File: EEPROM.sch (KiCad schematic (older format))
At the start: 0 parts

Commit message: EEPROM schematics were drawn
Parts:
- added C?: C_Small, Capacitor_SMD:C_0603_1608Metric_Pad1.08x0.95mm_HandSolder, symbol Device:C_Small
- added C?: 100nF, Capacitor_SMD:C_0603_1608Metric_Pad1.08x0.95mm_HandSolder, symbol Device:C_Small
- added C?: 30pF, Capacitor_SMD:C_0603_1608Metric_Pad1.08x0.95mm_HandSolder, symbol Device:C_Small
- added IC?: M24M02-DRMN6TP, SOIC127P600X175-8N, symbol GM_Memory_EEPROM:M24M02-DRMN6TP
- added R?: R_Small_US, Resistor_SMD:R_0603_1608Metric_Pad0.98x0.95mm_HandSolder, symbol Device:R_Small_US
- added R?: 0, Resistor_SMD:R_0603_1608Metric_Pad0.98x0.95mm_HandSolder, symbol Device:R_Small_US
- added R?: 4K, Resistor_SMD:R_0603_1608Metric_Pad0.98x0.95mm_HandSolder, symbol Device:R_Small_US
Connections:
- net labels added: +3V3, EEPROM_SCL, EEPROM_SDA, EEPROM_WC, GNDD, VCC3V3
- wire segments 0 -> 24
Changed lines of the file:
@@
 Comment4 ""
 $EndDescr
+$Comp
+L GM_Memory_EEPROM:M24M02-DRMN6TP IC?
+U 1 1 601D69D3
+P 3850 3300
+F 0 "IC?" H 4300 3465 50  0000 C CNN
+F 1 "M24M02-DRMN6TP" H 4300 3374 50  0000 C CNN
+F 2 "SOIC127P600X175-8N" H 5700 3500 50  0001 L CNN
+F 3 "http://www.st.com/content/ccc/resource/technical/document/datasheet/b7/de/9b/f6/03/28/4e/8e/CD00290537.pdf/files/CD00290537.pdf/jcr:content/translations/en.CD00290537.pdf" H 5700 3400 50  0001 L CNN
+F 4 "M24M02-DRMN6TP" H 3850 3300 50  0001 C CNN "MPN"
+	1    3850 3300
+	1    0    0    -1
+$EndComp
+$Comp
+L power:GNDD #PWR?
+U 1 1 601D83DB
+P 5150 4050
+AR Path="/601DF0A6/601D83DB" Ref="#PWR?"  Part="1"
+AR Path="/601E7C5A/601D83DB" Ref="#PWR?"  Part="1"
+F 0 "#PWR?" H 5150 3800 50  0001 C CNN
+F 1 "GNDD" H 5154 3895 50  0000 C CNN
+F 2 "" H 5150 4050 50  0001 C CNN
+F 3 "" H 5150 4050 50  0001 C CNN
+	1    5150 4050
+	1    0    0    -1
+$EndComp
+Wire Wire Line
+	4950 3700 5150 3700
+Wire Wire Line
+	5150 3700 5150 3800
+Wire Wire Line
+	4950 3900 5150 3900
+Connection ~ 5150 3900
+Wire Wire Line
+	5150 3900 5150 4050
+Wire Wire Line
+	4950 3800 5150 3800
+Connection ~ 5150 3800
+Wire Wire Line
+	5150 3800 5150 3900
+Wire Wire Line
+	4950 3400 6000 3400
+Wire Wire Line
+	3650 3400 3500 3400
+Wire Wire Line
+	3650 3800 2500 3800
+Wire Wire Line
+	3650 3900 2500 3900
+$Comp
+L Device:C_Small C?
+U 1 1 601D8FE6
+P 1250 1500
+F 0 "C?" H 1342 1546 50  0000 L CNN
+F 1 "C_Small" H 1342 1455 50  0000 L CNN
+F 2 "Capacitor_SMD:C_0603_1608Metric_Pad1.08x0.95mm_HandSolder" H 1250 1500 50  0001 C CNN
+F 3 "~" H 1250 1500 50  0001 C CNN
+F 4 "" H 1250 1500 50  0000 C CNN "Voltage"
+	1    1250 1500
+	1    0    0    -1
+$EndComp
+$Comp
+L Device:R_Small_US R?
+U 1 1 601D9F52
+P 1950 1500
+F 0 "R?" H 2018 1546 50  0000 L CNN
+F 1 "R_Small_US" H 2018 1455 50  0000 L CNN
+F 2 "Resistor_SMD:R_0603_1608Metric_Pad0.98x0.95mm_HandSolder" H 1950 1500 50  0001 C CNN
+F 3 "~" H 1950 1500 50  0001 C CNN
+	1    1950 1500
+	1    0    0    -1
+$EndComp
+$Comp
+L Device:C_Small C?
+U 1 1 601DC16C
+P 3100 3050
+F 0 "C?" H 3008 2959 50  0000 R CNN
+F 1 "100nF" H 3008 3050 50  0000 R CNN
+F 2 "Capacitor_SMD:C_0603_1608Metric_Pad1.08x0.95mm_HandSolder" H 3100 3050 50  0001 C CNN
+F 3 "~" H 3100 3050 50  0001 C CNN
+F 4 "25V" H 3008 3141 50  0000 R CNN "Voltage"
+	1    3100 3050
+	-1   0    0    1
+$EndComp
+Wire Wire Line
+	3100 2950 3100 2900
+Wire Wire Line
+	3100 2900 3500 2900
+$Comp
+L power:GNDD #PWR?
+U 1 1 601DF224
+P 3100 3200
+AR Path="/601DF0A6/601DF224" Ref="#PWR?"  Part="1"
+AR Path="/601E7C5A/601DF224" Ref="#PWR?"  Part="1"
+F 0 "#PWR?" H 3100 2950 50  0001 C CNN
+F 1 "GNDD" H 3104 3045 50  0000 C CNN
+F 2 "" H 3100 3200 50  0001 C CNN
+F 3 "" H 3100 3200 50  0001 C CNN
+	1    3100 3200
+	1    0    0    -1
+$EndComp
+Wire Wire Line
+	3100 3200 3100 3150
+Text Label 2750 3800 0    50   ~ 0
+EEPROM_SCL
+Text Label 2750 3900 0    50   ~ 0
+EEPROM_SDA
+Text Label 5250 3400 0    50   ~ 0
+EEPROM_WC
+Wire Wire Line
+	3500 2800 3500 2900
+Wire Wire Line
+	3500 2900 3500 3400
+$Comp
+L Device:R_Small_US R?
+U 1 1 601E53C9
+P 2850 3500
+F 0 "R?" V 3050 3500 50  0000 C CNN
+F 1 "0" V 2950 3500 50  0000 C CNN
+F 2 "Resistor_SMD:R_0603_1608Metric_Pad0.98x0.95mm_HandSolder" H 2850 3500 50  0001 C CNN
+F 3 "~" H 2850 3500 50  0001 C CNN
+F 4 "DNP" V 2750 3500 50  0000 C CNN "DNP"
+	1    2850 3500
+	0    -1   -1   0
+$EndComp
+Wire Wire Line
+	3650 3500 2950 3500
+$Comp
+L power:GNDD #PWR?
+U 1 1 601E70A9
+P 2500 3550
+AR Path="/601DF0A6/601E70A9" Ref="#PWR?"  Part="1"
+AR Path="/601E7C5A/601E70A9" Ref="#PWR?"  Part="1"
+F 0 "#PWR?" H 2500 3300 50  0001 C CNN
+F 1 "GNDD" H 2504 3395 50  0000 C CNN
+F 2 "" H 2500 3550 50  0001 C CNN
+F 3 "" H 2500 3550 50  0001 C CNN
+	1    2500 3550
+	1    0    0    -1
+$EndComp
+Wire Wire Line
+	2500 3500 2500 3550
+Wire Wire Line
+	2500 3500 2750 3500
+$Comp
+L Device:R_Small_US R?
+U 1 1 601EAD0F
+P 7900 3150
+F 0 "R?" H 7968 3196 50  0000 L CNN
+F 1 "4K" H 7968 3105 50  0000 L CNN
+F 2 "Resistor_SMD:R_0603_1608Metric_Pad0.98x0.95mm_HandSolder" H 7900 3150 50  0001 C CNN
+F 3 "~" H 7900 3150 50  0001 C CNN
+	1    7900 3150
+	1    0    0    -1
+$EndComp
+Wire Wire Line
+	7900 3250 7900 3400
+Wire Wire Line
+	7900 3050 7900 2900
+Wire Wire Line
+	7900 3750 7900 3950
+Wire Wire Line
+	7900 3400 9000 3400
+Connection ~ 7900 3400
+Text Label 8250 3400 0    50   ~ 0
+EEPROM_SDA
+Wire Wire Line
+	7900 3400 7900 3550
+$Comp
+L Device:C_Small C?
+U 1 1 601EAD09
+P 7900 3650
+F 0 "C?" H 7992 3741 50  0000 L CNN
+F 1 "30pF" H 7992 3650 50  0000 L CNN
+F 2 "Capacitor_SMD:C_0603_1608Metric_Pad1.08x0.95mm_HandSolder" H 7900 3650 50  0001 C CNN
+F 3 "~" H 7900 3650 50  0001 C CNN
+F 4 "25V" H 7992 3559 50  0000 L CNN "Voltage"
+	1    7900 3650
+	1    0    0    -1
+$EndComp
+$Comp
+L power:GNDD #PWR?
+U 1 1 601F091A
+P 7900 3950
+AR Path="/601DF0A6/601F091A" Ref="#PWR?"  Part="1"
+AR Path="/601E7C5A/601F091A" Ref="#PWR?"  Part="1"
+F 0 "#PWR?" H 7900 3700 50  0001 C CNN
+F 1 "GNDD" H 7904 3795 50  0000 C CNN
+F 2 "" H 7900 3950 50  0001 C CNN
+F 3 "" H 7900 3950 50  0001 C CNN
+	1    7900 3950
+	1    0    0    -1
+$EndComp
+$Comp
+L power:PWR_FLAG #FLG?
+U 1 1 601F6B98
+P 1250 1000
+AR Path="/601DF0A6/601F6B98" Ref="#FLG?"  Part="1"
+AR Path="/601E7C5A/601F6B98" Ref="#FLG?"  Part="1"
+F 0 "#FLG?" H 1250 1075 50  0001 C CNN
+F 1 "PWR_FLAG" H 1250 1173 50  0000 C CNN
+F 2 "" H 1250 1000 50  0001 C CNN
+F 3 "~" H 1250 1000 50  0001 C CNN
+	1    1250 1000
+	1    0    0    -1
+$EndComp
+Text GLabel 1050 1000 0    50   Input ~ 0
+VCC3V3
+Wire Wire Line
+	1050 1000 1250 1000
+Text HLabel 6000 3400 2    50   Input ~ 0
+EEPROM_WC
+Text HLabel 2500 3900 0    50   Input ~ 0
+EEPROM_SDA
+Text HLabel 2500 3800 0    50   Input ~ 0
+EEPROM_SCL
+$Comp
+L power:+3V3 #PWR?
+U 1 1 601FBA69
+P 3500 2800
+F 0 "#PWR?" H 3500 2650 50  0001 C CNN
+F 1 "+3V3" H 3515 2973 50  0000 C CNN
+F 2 "" H 3500 2800 50  0001 C CNN
+F 3 "" H 3500 2800 50  0001 C CNN
+	1    3500 2800
+	1    0    0    -1
+$EndComp
+$Comp
+L power:+3V3 #PWR?
+U 1 1 601FC8B2
+P 7900 2900
+F 0 "#PWR?" H 7900 2750 50  0001 C CNN
+F 1 "+3V3" H 7915 3073 50  0000 C CNN
+F 2 "" H 7900 2900 50  0001 C CNN
+F 3 "" H 7900 2900 50  0001 C CNN
+	1    7900 2900
+	1    0    0    -1
+$EndComp
+Connection ~ 3500 2900
 $EndSCHEMATC

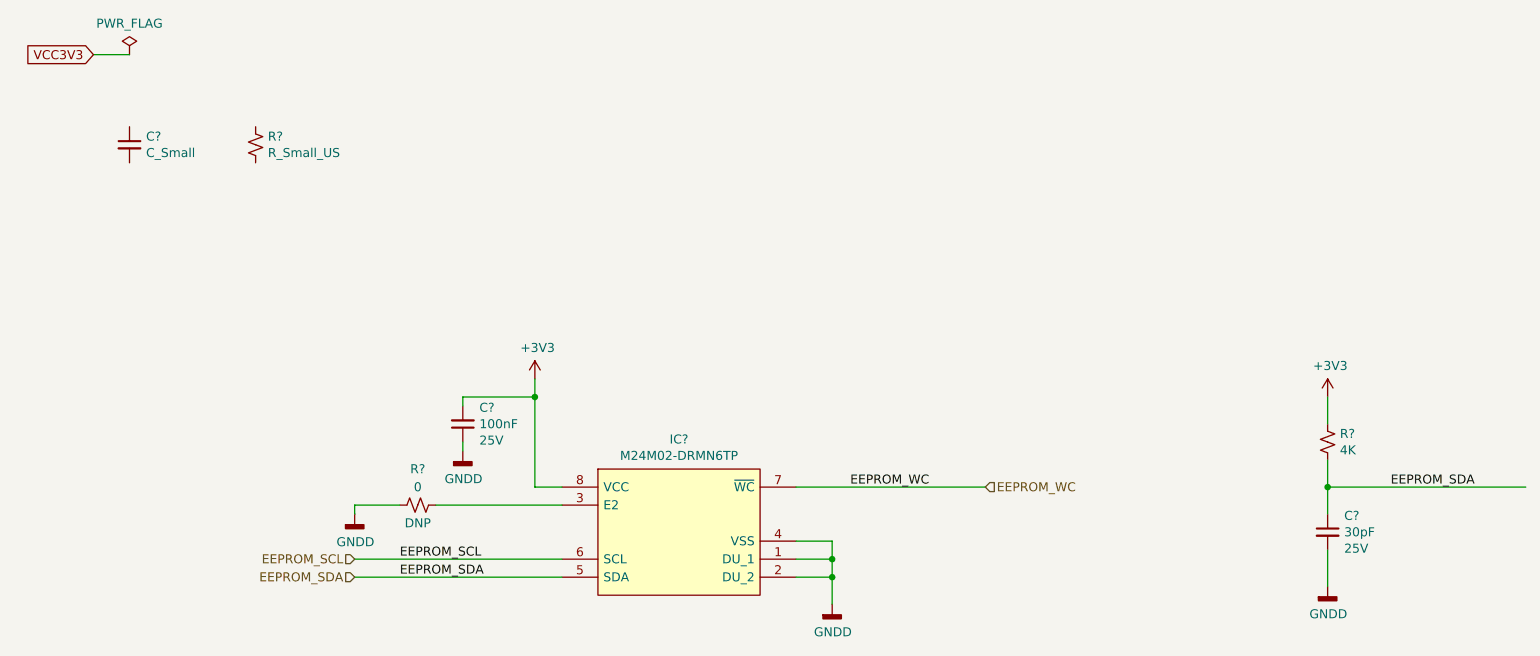
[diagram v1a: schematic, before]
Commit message: Completeed the FPGA_Power sheet Created PCB
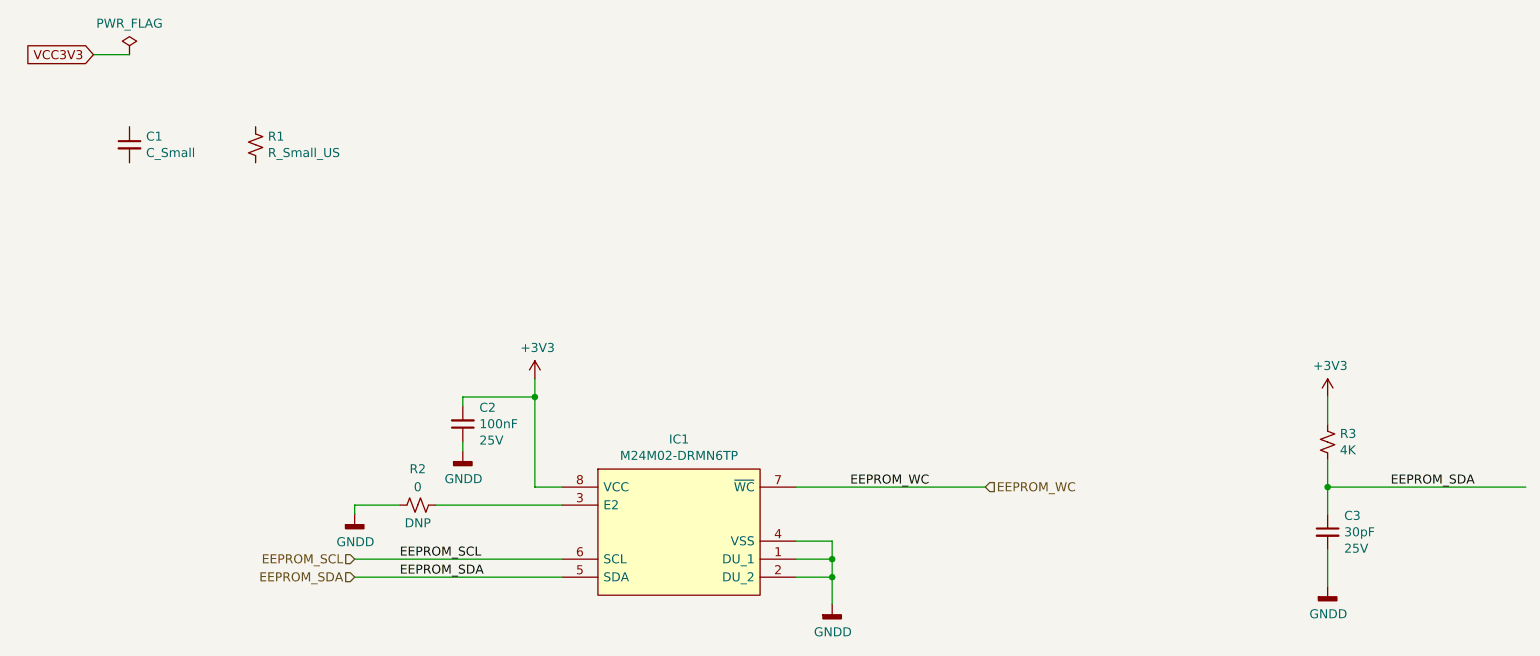
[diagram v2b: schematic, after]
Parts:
- gave numbers to parts that had none: 7
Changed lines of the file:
@@
 $EndDescr
 $Comp
-L GM_Memory_EEPROM:M24M02-DRMN6TP IC?
+L GM_Memory_EEPROM:M24M02-DRMN6TP IC1
 U 1 1 601D69D3
 P 3850 3300
-F 0 "IC?" H 4300 3465 50  0000 C CNN
+F 0 "IC1" H 4300 3465 50  0000 C CNN
 F 1 "M24M02-DRMN6TP" H 4300 3374 50  0000 C CNN
 F 2 "SOIC127P600X175-8N" H 5700 3500 50  0001 L CNN
@@
 P 5150 4050
 AR Path="/601DF0A6/601D83DB" Ref="#PWR?"  Part="1"
-AR Path="/601E7C5A/601D83DB" Ref="#PWR?"  Part="1"
-F 0 "#PWR?" H 5150 3800 50  0001 C CNN
+AR Path="/601E7C5A/601D83DB" Ref="#PWR04"  Part="1"
+F 0 "#PWR04" H 5150 3800 50  0001 C CNN
 F 1 "GNDD" H 5154 3895 50  0000 C CNN
 F 2 "" H 5150 4050 50  0001 C CNN
@@
 	3650 3900 2500 3900
 $Comp
-L Device:C_Small C?
+L Device:C_Small C1
 U 1 1 601D8FE6
 P 1250 1500
-F 0 "C?" H 1342 1546 50  0000 L CNN
+F 0 "C1" H 1342 1546 50  0000 L CNN
 F 1 "C_Small" H 1342 1455 50  0000 L CNN
 F 2 "Capacitor_SMD:C_0603_1608Metric_Pad1.08x0.95mm_HandSolder" H 1250 1500 50  0001 C CNN
@@
 $EndComp
 $Comp
-L Device:R_Small_US R?
+L Device:R_Small_US R1
 U 1 1 601D9F52
 P 1950 1500
-F 0 "R?" H 2018 1546 50  0000 L CNN
+F 0 "R1" H 2018 1546 50  0000 L CNN
 F 1 "R_Small_US" H 2018 1455 50  0000 L CNN
 F 2 "Resistor_SMD:R_0603_1608Metric_Pad0.98x0.95mm_HandSolder" H 1950 1500 50  0001 C CNN
@@
 $EndComp
 $Comp
-L Device:C_Small C?
+L Device:C_Small C2
 U 1 1 601DC16C
 P 3100 3050
-F 0 "C?" H 3008 2959 50  0000 R CNN
+F 0 "C2" H 3008 2959 50  0000 R CNN
 F 1 "100nF" H 3008 3050 50  0000 R CNN
 F 2 "Capacitor_SMD:C_0603_1608Metric_Pad1.08x0.95mm_HandSolder" H 3100 3050 50  0001 C CNN
@@
 P 3100 3200
 AR Path="/601DF0A6/601DF224" Ref="#PWR?"  Part="1"
-AR Path="/601E7C5A/601DF224" Ref="#PWR?"  Part="1"
-F 0 "#PWR?" H 3100 2950 50  0001 C CNN
+AR Path="/601E7C5A/601DF224" Ref="#PWR02"  Part="1"
+F 0 "#PWR02" H 3100 2950 50  0001 C CNN
 F 1 "GNDD" H 3104 3045 50  0000 C CNN
 F 2 "" H 3100 3200 50  0001 C CNN
@@
 	3500 2900 3500 3400
 $Comp
-L Device:R_Small_US R?
+L Device:R_Small_US R2
 U 1 1 601E53C9
 P 2850 3500
-F 0 "R?" V 3050 3500 50  0000 C CNN
+F 0 "R2" V 3050 3500 50  0000 C CNN
 F 1 "0" V 2950 3500 50  0000 C CNN
 F 2 "Resistor_SMD:R_0603_1608Metric_Pad0.98x0.95mm_HandSolder" H 2850 3500 50  0001 C CNN
@@
 P 2500 3550
 AR Path="/601DF0A6/601E70A9" Ref="#PWR?"  Part="1"
-AR Path="/601E7C5A/601E70A9" Ref="#PWR?"  Part="1"
-F 0 "#PWR?" H 2500 3300 50  0001 C CNN
+AR Path="/601E7C5A/601E70A9" Ref="#PWR01"  Part="1"
+F 0 "#PWR01" H 2500 3300 50  0001 C CNN
 F 1 "GNDD" H 2504 3395 50  0000 C CNN
 F 2 "" H 2500 3550 50  0001 C CNN
@@
 	2500 3500 2750 3500
 $Comp
-L Device:R_Small_US R?
+L Device:R_Small_US R3
 U 1 1 601EAD0F
 P 7900 3150
-F 0 "R?" H 7968 3196 50  0000 L CNN
+F 0 "R3" H 7968 3196 50  0000 L CNN
 F 1 "4K" H 7968 3105 50  0000 L CNN
 F 2 "Resistor_SMD:R_0603_1608Metric_Pad0.98x0.95mm_HandSolder" H 7900 3150 50  0001 C CNN
@@
 	7900 3400 7900 3550
 $Comp
-L Device:C_Small C?
+L Device:C_Small C3
 U 1 1 601EAD09
 P 7900 3650
-F 0 "C?" H 7992 3741 50  0000 L CNN
+F 0 "C3" H 7992 3741 50  0000 L CNN
 F 1 "30pF" H 7992 3650 50  0000 L CNN
 F 2 "Capacitor_SMD:C_0603_1608Metric_Pad1.08x0.95mm_HandSolder" H 7900 3650 50  0001 C CNN
@@
 P 7900 3950
 AR Path="/601DF0A6/601F091A" Ref="#PWR?"  Part="1"
-AR Path="/601E7C5A/601F091A" Ref="#PWR?"  Part="1"
-F 0 "#PWR?" H 7900 3700 50  0001 C CNN
+AR Path="/601E7C5A/601F091A" Ref="#PWR06"  Part="1"
+F 0 "#PWR06" H 7900 3700 50  0001 C CNN
 F 1 "GNDD" H 7904 3795 50  0000 C CNN
 F 2 "" H 7900 3950 50  0001 C CNN
@@
 P 1250 1000
 AR Path="/601DF0A6/601F6B98" Ref="#FLG?"  Part="1"
-AR Path="/601E7C5A/601F6B98" Ref="#FLG?"  Part="1"
-F 0 "#FLG?" H 1250 1075 50  0001 C CNN
+AR Path="/601E7C5A/601F6B98" Ref="#FLG01"  Part="1"
+F 0 "#FLG01" H 1250 1075 50  0001 C CNN
 F 1 "PWR_FLAG" H 1250 1173 50  0000 C CNN
 F 2 "" H 1250 1000 50  0001 C CNN
@@
 EEPROM_SCL
 $Comp
-L power:+3V3 #PWR?
+L power:+3V3 #PWR03
 U 1 1 601FBA69
 P 3500 2800
-F 0 "#PWR?" H 3500 2650 50  0001 C CNN
+F 0 "#PWR03" H 3500 2650 50  0001 C CNN
 F 1 "+3V3" H 3515 2973 50  0000 C CNN
 F 2 "" H 3500 2800 50  0001 C CNN
@@
 $EndComp
 $Comp
-L power:+3V3 #PWR?
+L power:+3V3 #PWR05
 U 1 1 601FC8B2
 P 7900 2900
-F 0 "#PWR?" H 7900 2750 50  0001 C CNN
+F 0 "#PWR05" H 7900 2750 50  0001 C CNN
 F 1 "+3V3" H 7915 3073 50  0000 C CNN
 F 2 "" H 7900 2900 50  0001 C CNN

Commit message: Added power symbol to EEPROM sheet
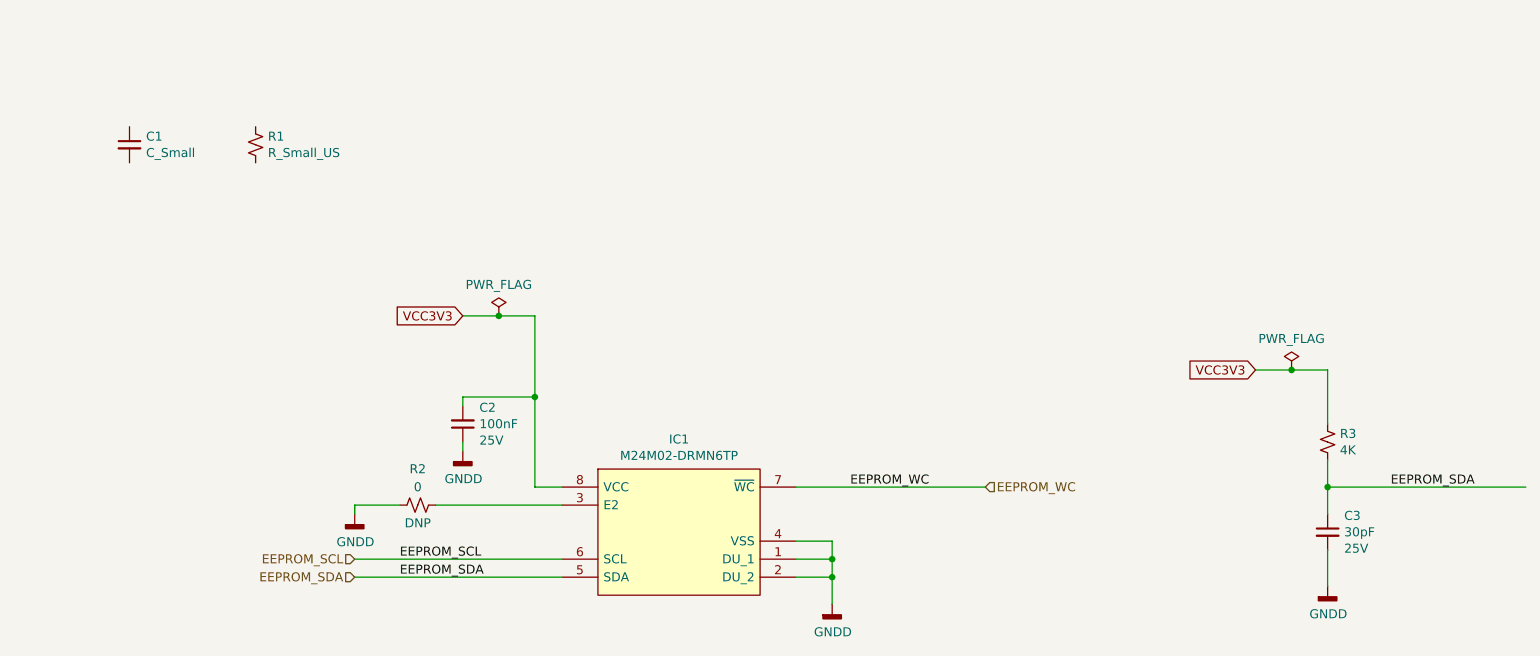
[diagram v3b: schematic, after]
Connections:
- net labels removed: +3V3
- wire segments 24 -> 27
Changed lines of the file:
@@
 EEPROM_WC
-Wire Wire Line
-	3500 2800 3500 2900
 Wire Wire Line
 	3500 2900 3500 3400
@@
 	7900 3250 7900 3400
 Wire Wire Line
-	7900 3050 7900 2900
-Wire Wire Line
 	7900 3750 7900 3950
 Wire Wire Line
@@
 	1    0    0    -1
 $EndComp
-$Comp
-L power:PWR_FLAG #FLG?
-U 1 1 601F6B98
-P 1250 1000
-AR Path="/601DF0A6/601F6B98" Ref="#FLG?"  Part="1"
-AR Path="/601E7C5A/601F6B98" Ref="#FLG01"  Part="1"
-F 0 "#FLG01" H 1250 1075 50  0001 C CNN
-F 1 "PWR_FLAG" H 1250 1173 50  0000 C CNN
-F 2 "" H 1250 1000 50  0001 C CNN
-F 3 "~" H 1250 1000 50  0001 C CNN
-	1    1250 1000
-	1    0    0    -1
-$EndComp
-Text GLabel 1050 1000 0    50   Input ~ 0
-VCC3V3
-Wire Wire Line
-	1050 1000 1250 1000
 Text HLabel 6000 3400 2    50   Input ~ 0
 EEPROM_WC
@@
 Text HLabel 2500 3800 0    50   Input ~ 0
 EEPROM_SCL
+Connection ~ 3500 2900
+Text GLabel 3100 2450 0    50   Input ~ 0
+VCC3V3
 $Comp
-L power:+3V3 #PWR03
-U 1 1 601FBA69
-P 3500 2800
-F 0 "#PWR03" H 3500 2650 50  0001 C CNN
-F 1 "+3V3" H 3515 2973 50  0000 C CNN
-F 2 "" H 3500 2800 50  0001 C CNN
-F 3 "" H 3500 2800 50  0001 C CNN
-	1    3500 2800
+L power:PWR_FLAG #FLG?
+U 1 1 60222E62
+P 3300 2450
+F 0 "#FLG?" H 3300 2525 50  0001 C CNN
+F 1 "PWR_FLAG" H 3300 2623 50  0000 C CNN
+F 2 "" H 3300 2450 50  0001 C CNN
+F 3 "~" H 3300 2450 50  0001 C CNN
+	1    3300 2450
 	1    0    0    -1
 $EndComp
+Wire Wire Line
+	3500 2450 3500 2900
+Connection ~ 3300 2450
+Wire Wire Line
+	3300 2450 3500 2450
+Wire Wire Line
+	3100 2450 3300 2450
+Text GLabel 7500 2750 0    50   Input ~ 0
+VCC3V3
 $Comp
-L power:+3V3 #PWR05
-U 1 1 601FC8B2
-P 7900 2900
-F 0 "#PWR05" H 7900 2750 50  0001 C CNN
-F 1 "+3V3" H 7915 3073 50  0000 C CNN
-F 2 "" H 7900 2900 50  0001 C CNN
-F 3 "" H 7900 2900 50  0001 C CNN
-	1    7900 2900
+L power:PWR_FLAG #FLG?
+U 1 1 602261D1
+P 7700 2750
+F 0 "#FLG?" H 7700 2825 50  0001 C CNN
+F 1 "PWR_FLAG" H 7700 2923 50  0000 C CNN
+F 2 "" H 7700 2750 50  0001 C CNN
+F 3 "~" H 7700 2750 50  0001 C CNN
+	1    7700 2750
 	1    0    0    -1
 $EndComp
-Connection ~ 3500 2900
+Connection ~ 7700 2750
+Wire Wire Line
+	7700 2750 7900 2750
+Wire Wire Line
+	7500 2750 7700 2750
+Wire Wire Line
+	7900 2750 7900 3050
 $EndSCHEMATC
